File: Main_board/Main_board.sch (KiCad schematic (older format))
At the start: 60 parts, among them U1 ATmega328-AU, U2 74LVC2G08, U3 74LVC2G08, Y1 20Mhz

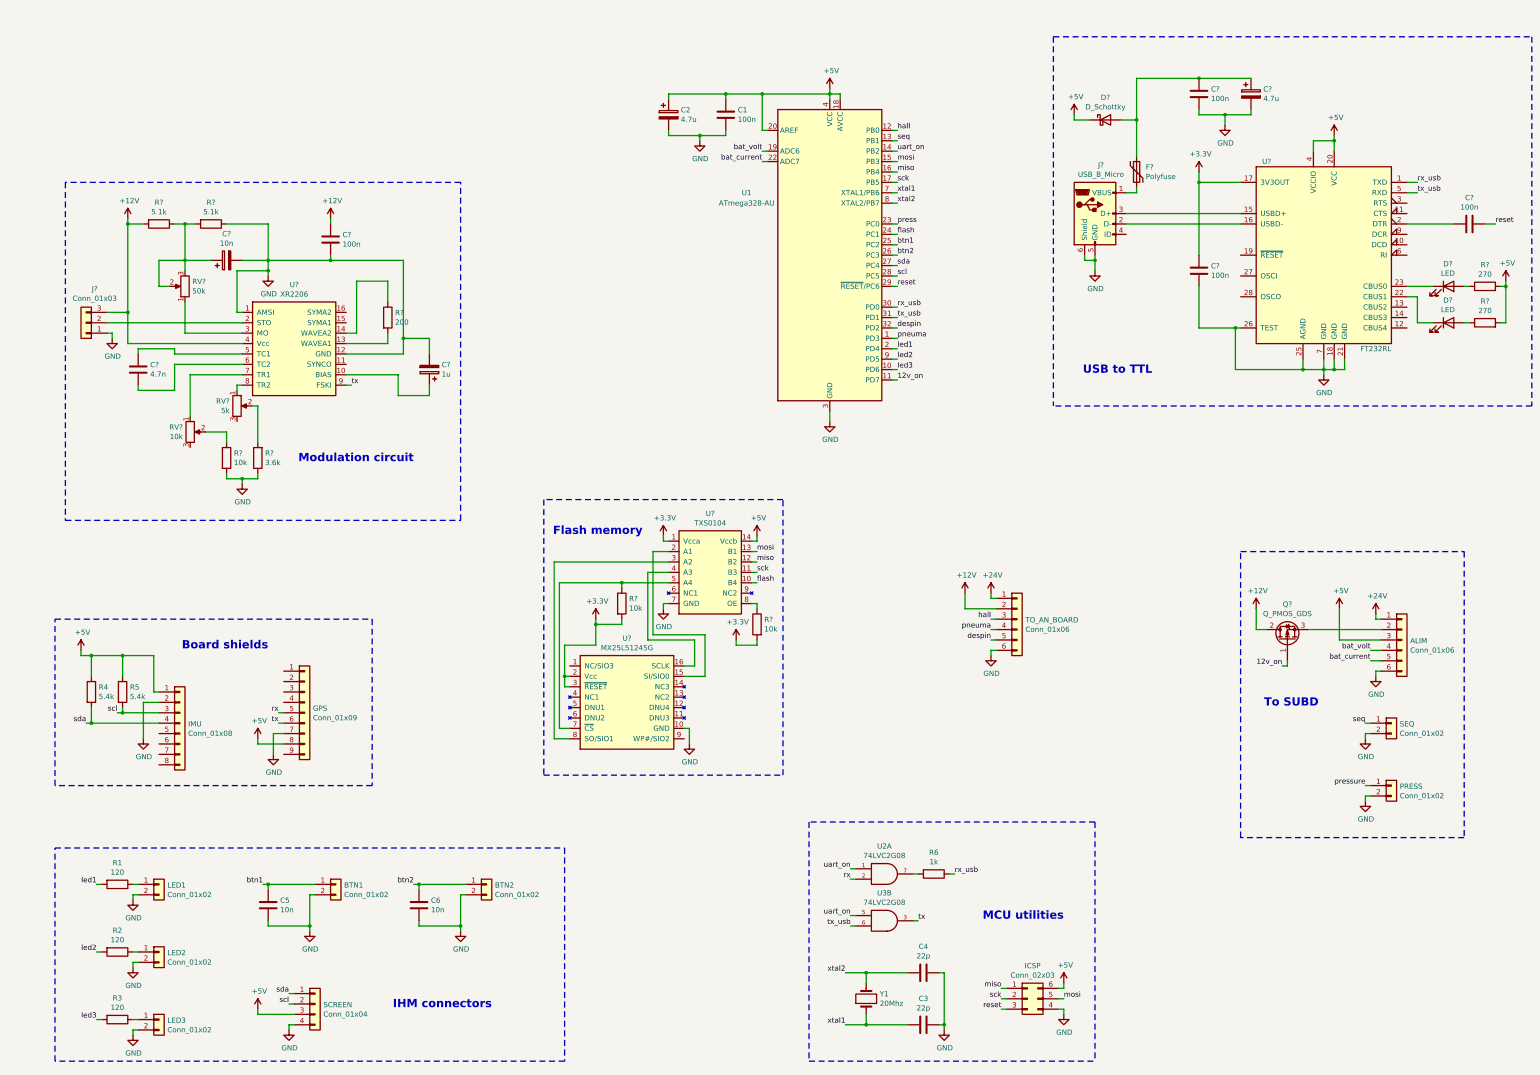
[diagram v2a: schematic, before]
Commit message: ENH: Added UART multichannel handling + style update
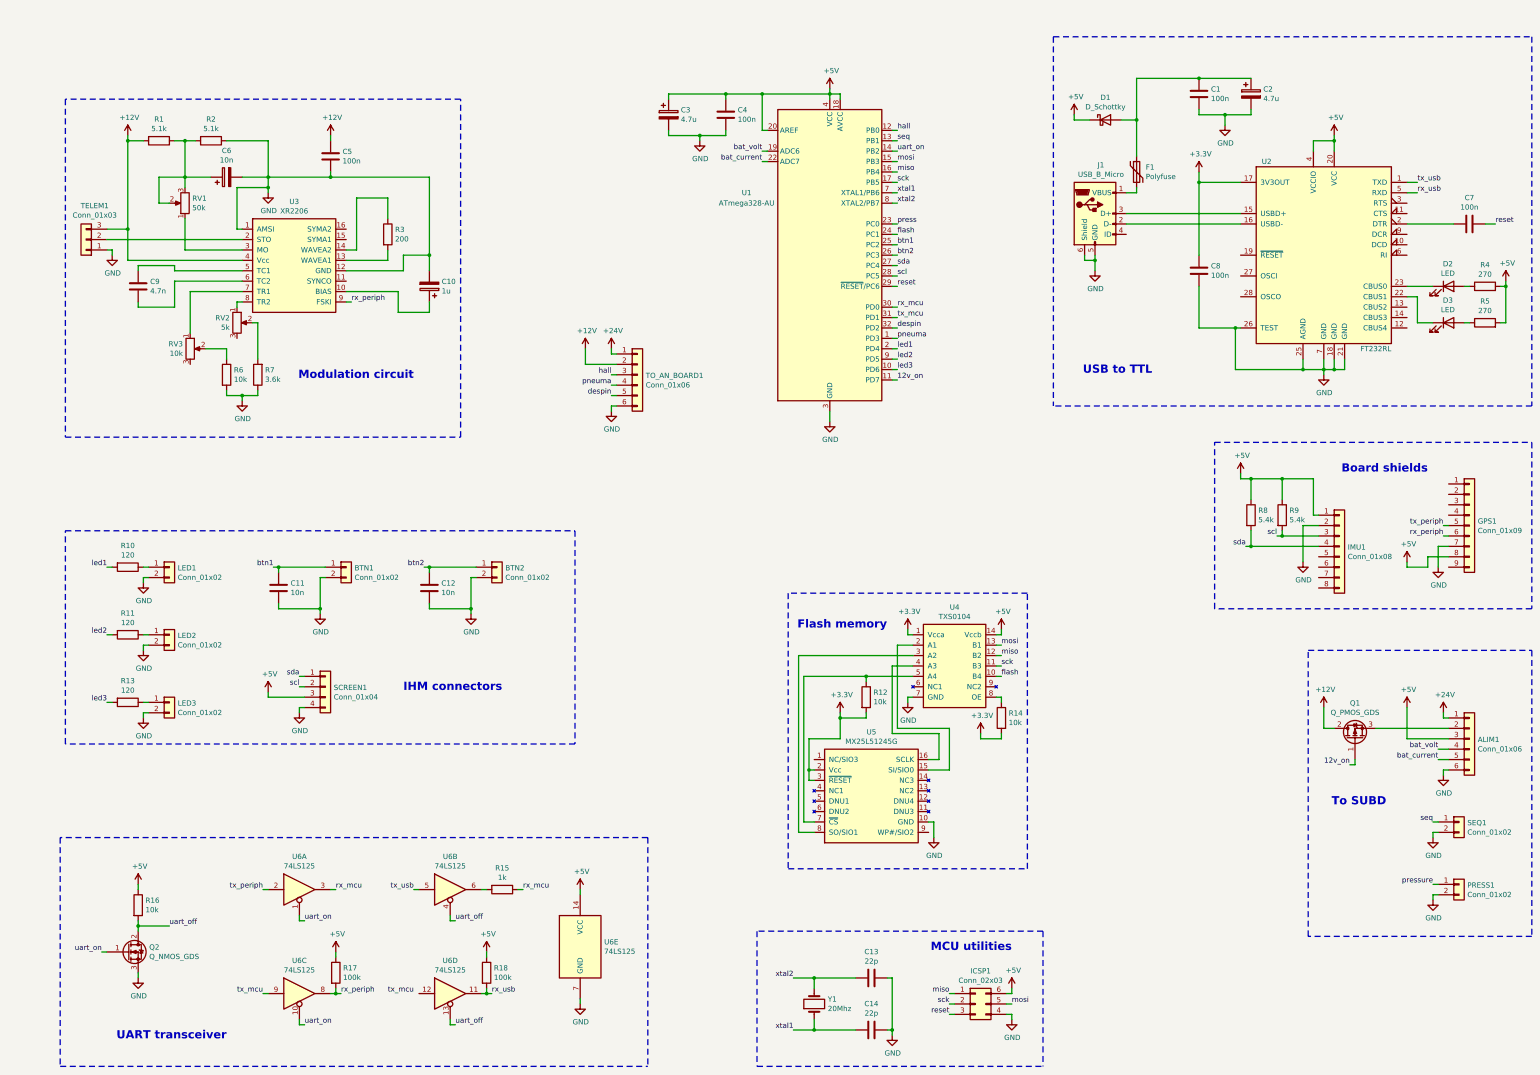
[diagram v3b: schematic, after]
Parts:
- removed R6: 1k, symbol Device:R
- removed U2, U3: 74LVC2G08, symbol 74xGxx:74LVC2G08
- added Q2: Q_NMOS_GDS, symbol Device:Q_NMOS_GDS
- added R15: 1k, symbol Device:R
- added R16: 10k, symbol Device:R
- added R17, R18: 100k, symbol Device:R
- added U6: 74LS125, symbol 74xx:74LS125
- ALIM1: renamed from ALIM; footprint (none) -> Connector_PinHeader_2.54mm:PinHeader_1x06_P2.54mm_Vertical
- BTN1, BTN2, LED1, LED2, LED3: footprint (none) -> Connector_PinHeader_2.54mm:PinHeader_1x02_P2.54mm_Vertical
- ICSP1: renamed from ICSP; footprint (none) -> Connector_PinHeader_2.54mm:PinHeader_2x03_P2.54mm_Vertical
- PRESS1: renamed from PRESS; footprint (none) -> Connector_PinHeader_2.54mm:PinHeader_1x02_P2.54mm_Vertical
- SCREEN1: renamed from SCREEN; footprint (none) -> Connector_PinHeader_2.54mm:PinHeader_1x04_P2.54mm_Vertical
- SEQ1: renamed from SEQ; footprint (none) -> Connector_PinHeader_2.54mm:PinHeader_1x02_P2.54mm_Vertical
- TO_AN_BOARD1: renamed from TO_AN_BOARD; footprint (none) -> Connector_PinHeader_2.54mm:PinHeader_1x06_P2.54mm_Vertical
- gave numbers to parts that had none: 31
- renumbered C5 to C11, C6 to C12, C4 to C13, C3 to C14, C2 to C3, C1 to C4, GPS to GPS1, IMU to IMU1, R1 to R10, R2 to R11, R3 to R13, R4 to R8, R5 to R9
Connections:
- net +5V: now also R16.1, R17.1, R18.1, U6.14 (VCC)
- net GND: now also Q2.3 (S), U6.7 (GND)
- net rx_usb: now also U2.5 (RXD), R18.2, U6.11; no longer U1.30 (PD0), U2.1 (TXD)
- net tx_usb: now also U2.1 (TXD), U6.5; no longer U1.31 (PD1), U2.5 (RXD)
- net uart_on: now also Q2.1 (G), U6.1, U6.10
- net rx renamed tx_periph
- net tx_periph: now also U6.2
- net tx renamed rx_periph
- net rx_periph: now also R17.2, U6.8
- new net: R15.2, U6.6
- new net rx_mcu: R15.1, U1.30 (PD0), U6.3
- new net tx_mcu: U1.31 (PD1), U6.9
- new net uart_off: Q2.2 (D), R16.2, U6.13, U6.4
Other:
- note added: "UART transceiver"
- moved on the sheet: ALIM1, BTN1, BTN2, C10, C11, C12, C13, C14, C5, C6, C9, GPS1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

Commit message: ENH: Added most of the footprints (GPS+IMU remaining) + added 5v led
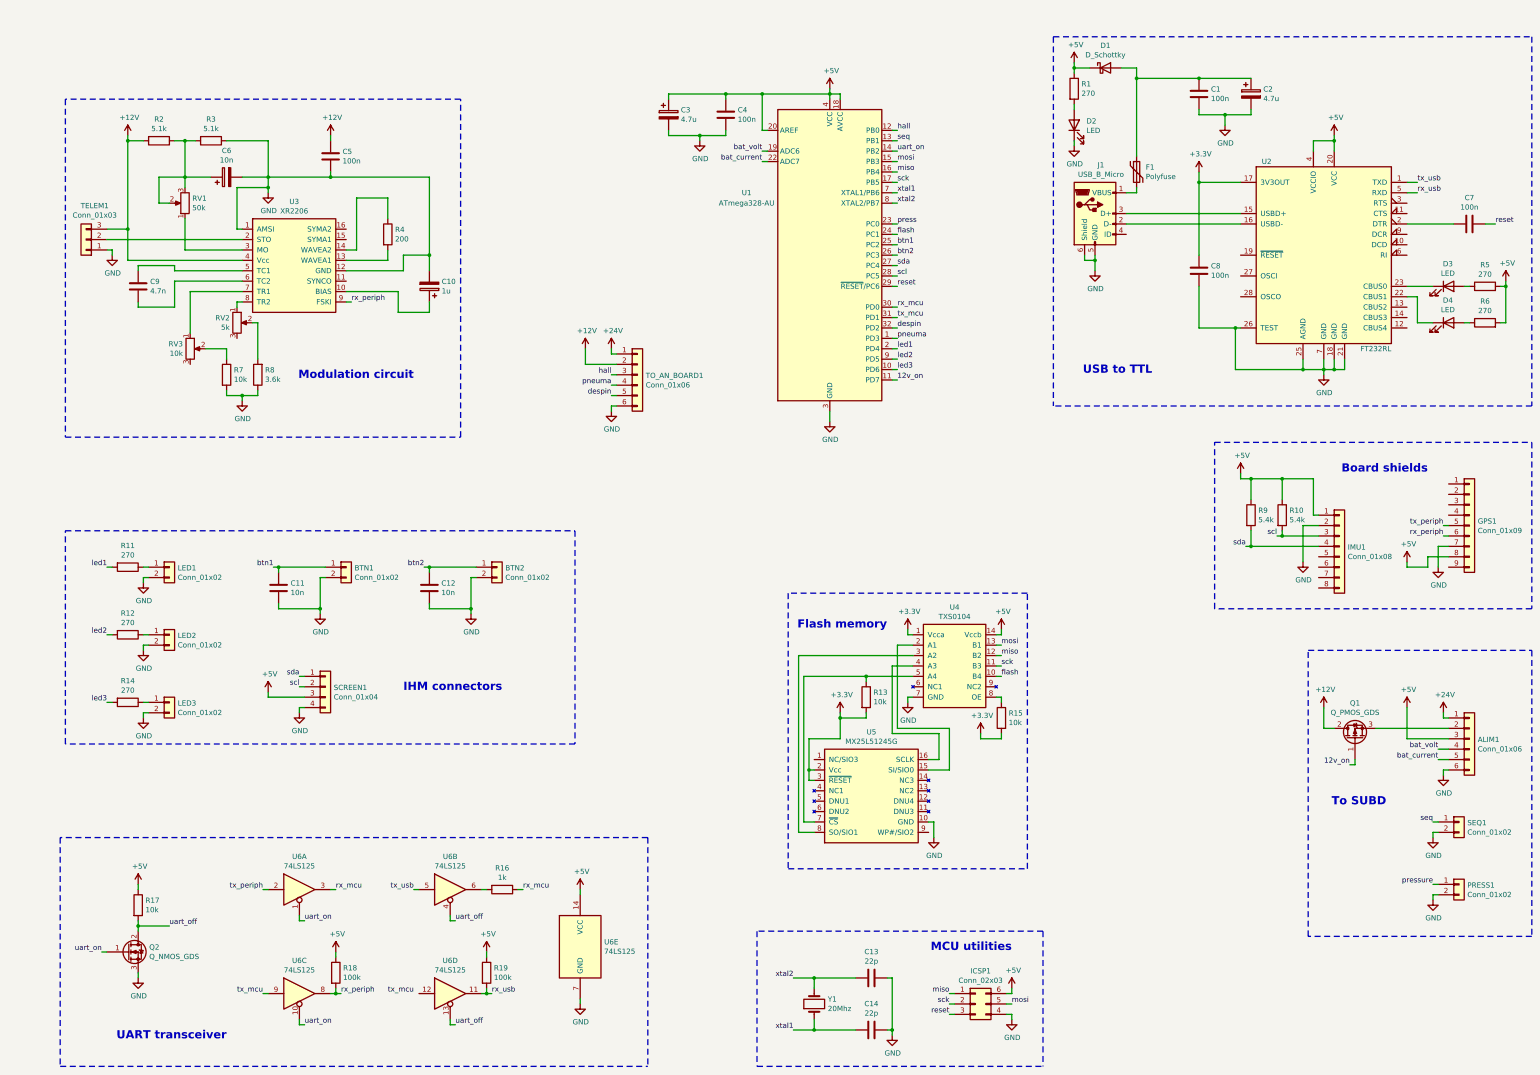
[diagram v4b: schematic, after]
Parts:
- added D2: LED, LED_SMD:LED_0805_2012Metric, symbol Device:LED
- added R1: 270, Resistor_SMD:R_0603_1608Metric, symbol Device:R
- C1, C13, C14, C4, C5, C7, C8: footprint (none) -> Capacitor_SMD:C_0603_1608Metric
- C10, C2, C3, C9: footprint (none) -> Capacitor_SMD:CP_Elec_4x5.4
- C11, C12, C6: footprint (none) -> Capacitor_SMD:C_1206_3216Metric
- D1: footprint (none) -> Diode_SMD:D_SOD-123F
- D3: renamed from D2; footprint (none) -> LED_SMD:LED_0805_2012Metric
- D4: renamed from D3; footprint (none) -> LED_SMD:LED_0805_2012Metric
- F1: footprint (none) -> Fuse:Fuse_1812_4532Metric
- Q1, Q2: footprint (none) -> Package_TO_SOT_SMD:TO-252-2
- R10: renamed from R9; footprint (none) -> Resistor_SMD:R_0603_1608Metric
- R11: renamed from R10; value 120 -> 270; footprint (none) -> Resistor_SMD:R_0603_1608Metric
- R12: renamed from R11; value 120 -> 270; footprint (none) -> Resistor_SMD:R_0603_1608Metric
- R13: renamed from R12; footprint (none) -> Resistor_SMD:R_0603_1608Metric
- R14: renamed from R13; value 120 -> 270; footprint (none) -> Resistor_SMD:R_0603_1608Metric
- R15: renamed from R14; footprint (none) -> Resistor_SMD:R_0603_1608Metric
- R16: renamed from R15; footprint (none) -> Resistor_SMD:R_0603_1608Metric
- R17: renamed from R16; footprint (none) -> Resistor_SMD:R_0603_1608Metric
- R18: renamed from R17; footprint (none) -> Resistor_SMD:R_0603_1608Metric
- R19: renamed from R18; footprint (none) -> Resistor_SMD:R_0603_1608Metric
- R2: renamed from R1; footprint (none) -> Resistor_SMD:R_0603_1608Metric
- R3: renamed from R2; footprint (none) -> Resistor_SMD:R_0603_1608Metric
- R4: renamed from R3; footprint (none) -> Resistor_SMD:R_0603_1608Metric
- R5: renamed from R4; footprint (none) -> Resistor_SMD:R_0603_1608Metric
- R6: renamed from R5; footprint (none) -> Resistor_SMD:R_0603_1608Metric
- R7: renamed from R6; footprint (none) -> Resistor_SMD:R_0603_1608Metric
- R8: renamed from R7; footprint (none) -> Resistor_SMD:R_0603_1608Metric
- R9: renamed from R8; footprint (none) -> Resistor_SMD:R_0603_1608Metric
- RV1, RV2, RV3: footprint (none) -> Potentiometer_THT:Potentiometer_Bourns_3296W_Vertical
- TELEM1: footprint (none) -> Connector_PinHeader_2.54mm:PinHeader_1x03_P2.54mm_Vertical
- U6: footprint (none) -> Package_SO:SOIC-14_3.9x8.7mm_P1.27mm
- Y1: footprint (none) -> Crystal:Crystal_HC49-4H_Vertical
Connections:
- net +5V: now also R1.1
- net GND: now also D2.1 (K)
- new net: D2.2 (A), R1.2
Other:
- moved on the sheet: D1

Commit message: ENH: Added MPU6050 footprint
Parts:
- GPS1: footprint (none) -> SHIELD_GPS_ADAFRUIT:SHIELD_GPS_ADAFRUIT
- IMU1: footprint (none) -> SHIELD_MPU_6050:SHIELD_MPU_6050
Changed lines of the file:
@@
 F 0 "IMU1" H 13630 5692 50  0000 L CNN
 F 1 "Conn_01x08" H 13630 5601 50  0000 L CNN
-F 2 "" H 13550 5700 50  0001 C CNN
+F 2 "SHIELD_MPU_6050:SHIELD_MPU_6050" H 13550 5700 50  0001 C CNN
 F 3 "~" H 13550 5700 50  0001 C CNN
 	1    13550 5700
@@
 F 0 "GPS1" H 14880 5542 50  0000 L CNN
 F 1 "Conn_01x09" H 14880 5451 50  0000 L CNN
-F 2 "" H 14800 5500 50  0001 C CNN
+F 2 "SHIELD_GPS_ADAFRUIT:SHIELD_GPS_ADAFRUIT" H 14800 5500 50  0001 C CNN
 F 3 "~" H 14800 5500 50  0001 C CNN
 	1    14800 5500
